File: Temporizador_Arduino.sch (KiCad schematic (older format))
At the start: 9 parts, among them Q1 BC 548

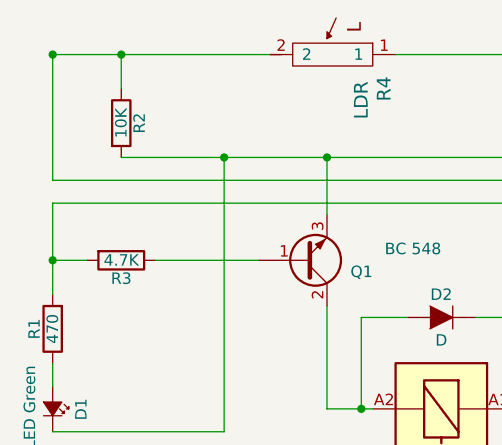
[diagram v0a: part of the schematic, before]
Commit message: Adiciona PDF com esquema eletrico
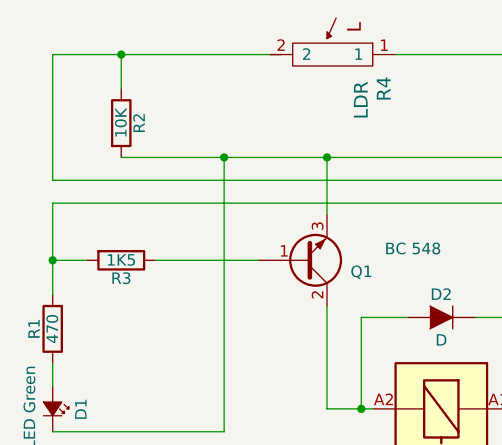
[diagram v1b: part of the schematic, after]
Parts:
- R3: value 4.7K -> 1K5
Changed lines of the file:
@@
 P 1900 1800
 F 0 "R3" V 1980 1800 50  0000 C CNN
-F 1 "4.7K" V 1900 1800 50  0000 C CNN
+F 1 "1K5" V 1900 1800 50  0000 C CNN
 F 2 "rc-master:rc-master-0204%2f5" V 1830 1800 30  0001 C CNN
 F 3 "" H 1900 1800 30  0000 C CNN
@@
 Wire Wire Line
 	1600 1450 1600 900
-Connection ~ 1600 900
 Wire Wire Line
 	1600 1550 4300 1550

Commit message: Correcao na rotina de tempo e imagem com esquema eletrico
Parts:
- CONN1: symbol Connector -> Connector-RESCUE-Temporizador_Arduino
- D1: value LED Green -> LED Verde
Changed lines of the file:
@@
 EESchema Schematic File Version 2
+LIBS:Temporizador_Arduino-rescue
 LIBS:Connector
 LIBS:power
@@
 P 1600 2450
 F 0 "D1" H 1550 2575 50  0000 L CNN
-F 1 "LED Green" H 1425 2350 50  0000 L CNN
+F 1 "LED Verde" H 1425 2350 50  0000 L CNN
 F 2 "led:led-LED3MM" V 1600 2450 60  0001 C CNN
 F 3 "" V 1600 2450 60  0000 C CNN
@@
 	3800 1650 4300 1650
 $Comp
-L Connector CONN1
+L Connector-RESCUE-Temporizador_Arduino CONN1
 U 1 1 566CDDE4
 P 4700 1100
